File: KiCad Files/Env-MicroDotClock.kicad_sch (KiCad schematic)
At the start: 40 parts, among them IC1 IS31FL3730-QFLS2-TR, IC2 IS31FL3730-QFLS2-TR, IC3 IS31FL3730-QFLS2-TR, IC4 IS31FL3730-QFLS2-TR, M1 LTP-305G, M2 LTP-305G, M3 LTP-305G, M4 LTP-305G, M5 LTP-305G, M6 LTP-305G, M7 LTP-305G, M8 LTP-305G, Q1 2SC1815, SW1 SW_Push, SW2 SW_Push, SW3 SW_Push, SW4 SW_Push, U1 Pico, U2 DS1307Z+, Y1 32.768kHz 45kΩ 12.5

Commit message: small changes and fixes, among other adjustments.
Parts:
- removed Q1: 2SC1815, Package_TO_SOT_THT:TO-92_Inline, symbol Transistor_BJT:2SC1815
- removed U2: DS1307Z+, Package_SO:SOIC-8_3.9x4.9mm_P1.27mm, symbol Timer_RTC:DS1307Z+
- removed Y1: 32.768kHz 45kΩ 12.5, Crystal:Crystal_SMD_3225-4Pin_3.2x2.5mm_HandSoldering, symbol Device:Crystal_GND24
- added Q1: 2SC1815, Package_TO_SOT_SMD:SOT-23, symbol Transistor_BJT:BC817
- added U3: DS3231M, Package_SO:SOIC-16W_7.5x10.3mm_P1.27mm, symbol Timer_RTC:DS3231M
- C10: value 0805 15pF -> 0805 1uF
- C9: value 0805 15pF -> 0805 0.1uF
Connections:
- net +5V: now also C10.1, C9.1, U3.2 (VCC)
- net GND: now also C10.2, C9.2, Q1.2 (E), U3.10 (GND), U3.11 (GND), U3.12 (GND), U3.13 (GND), U3.5 (GND), U3.6 (GND), U3.7 (GND), U3.8 (GND), U3.9 (GND); no longer C10.1, C9.1
- net I2C_SCL: now also U3.16 (SCL)
- net I2C_SDA: now also U3.15 (SDA)
- net at R4.2: now also Q1.1 (B)
- net at BZ1.2 (+), R3.2: now also Q1.3 (C)
- net at BT1.1 (+): now also U3.14 (VBAT)

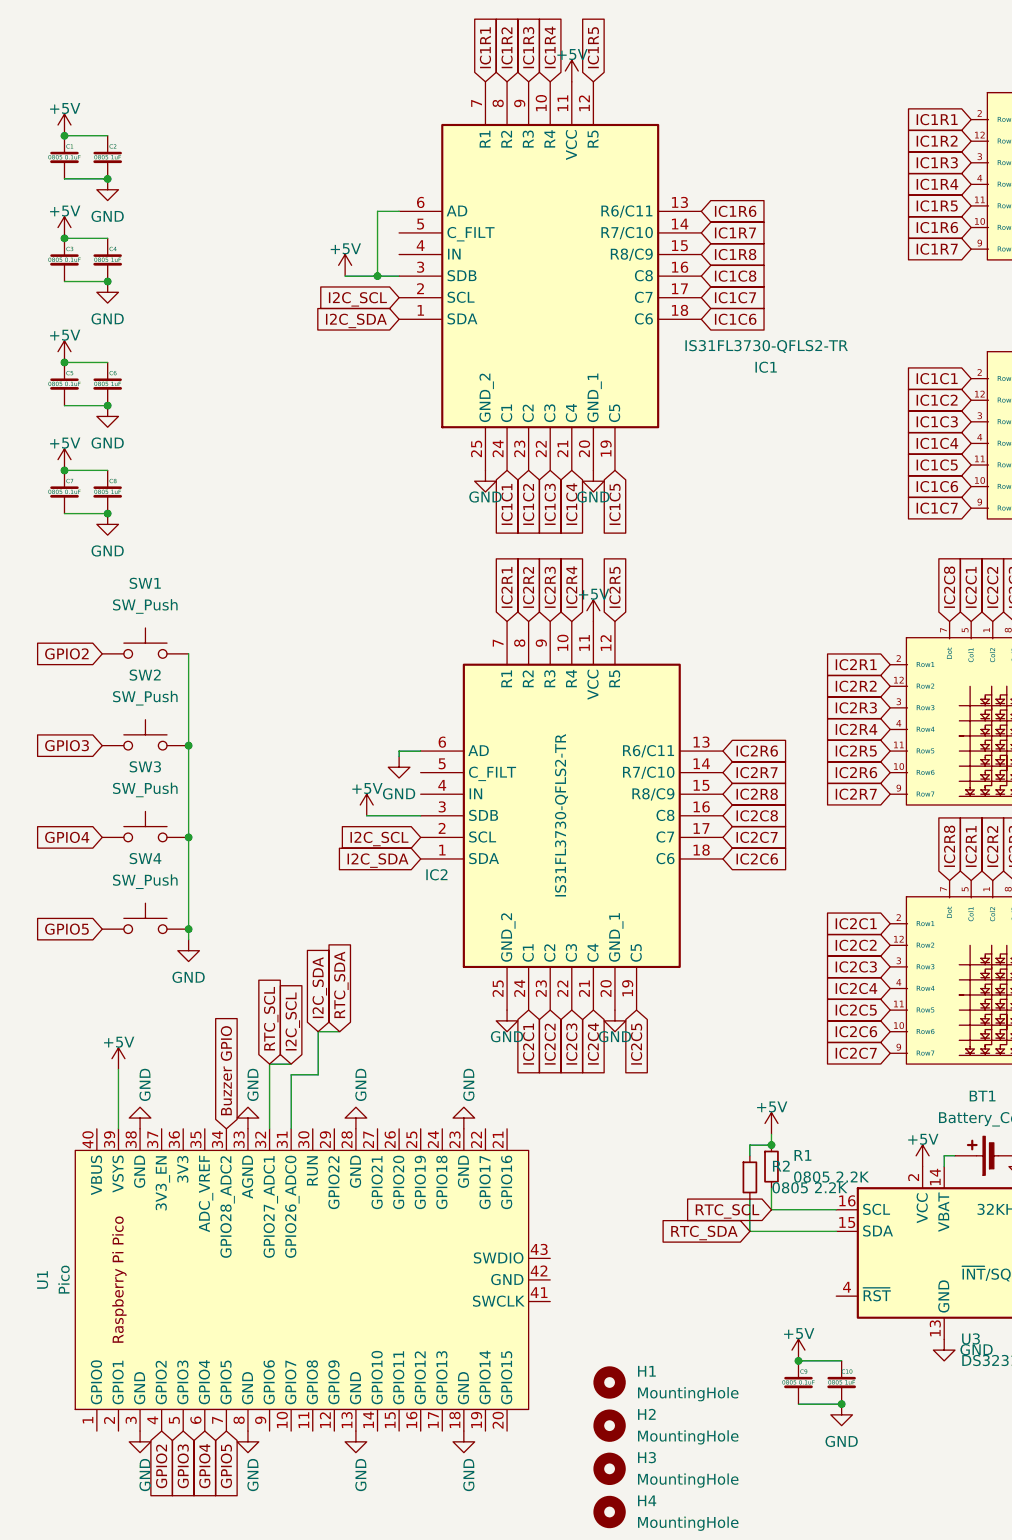
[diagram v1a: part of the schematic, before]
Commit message: Moved LTP305s up and the matrix ICs below the LTP305s
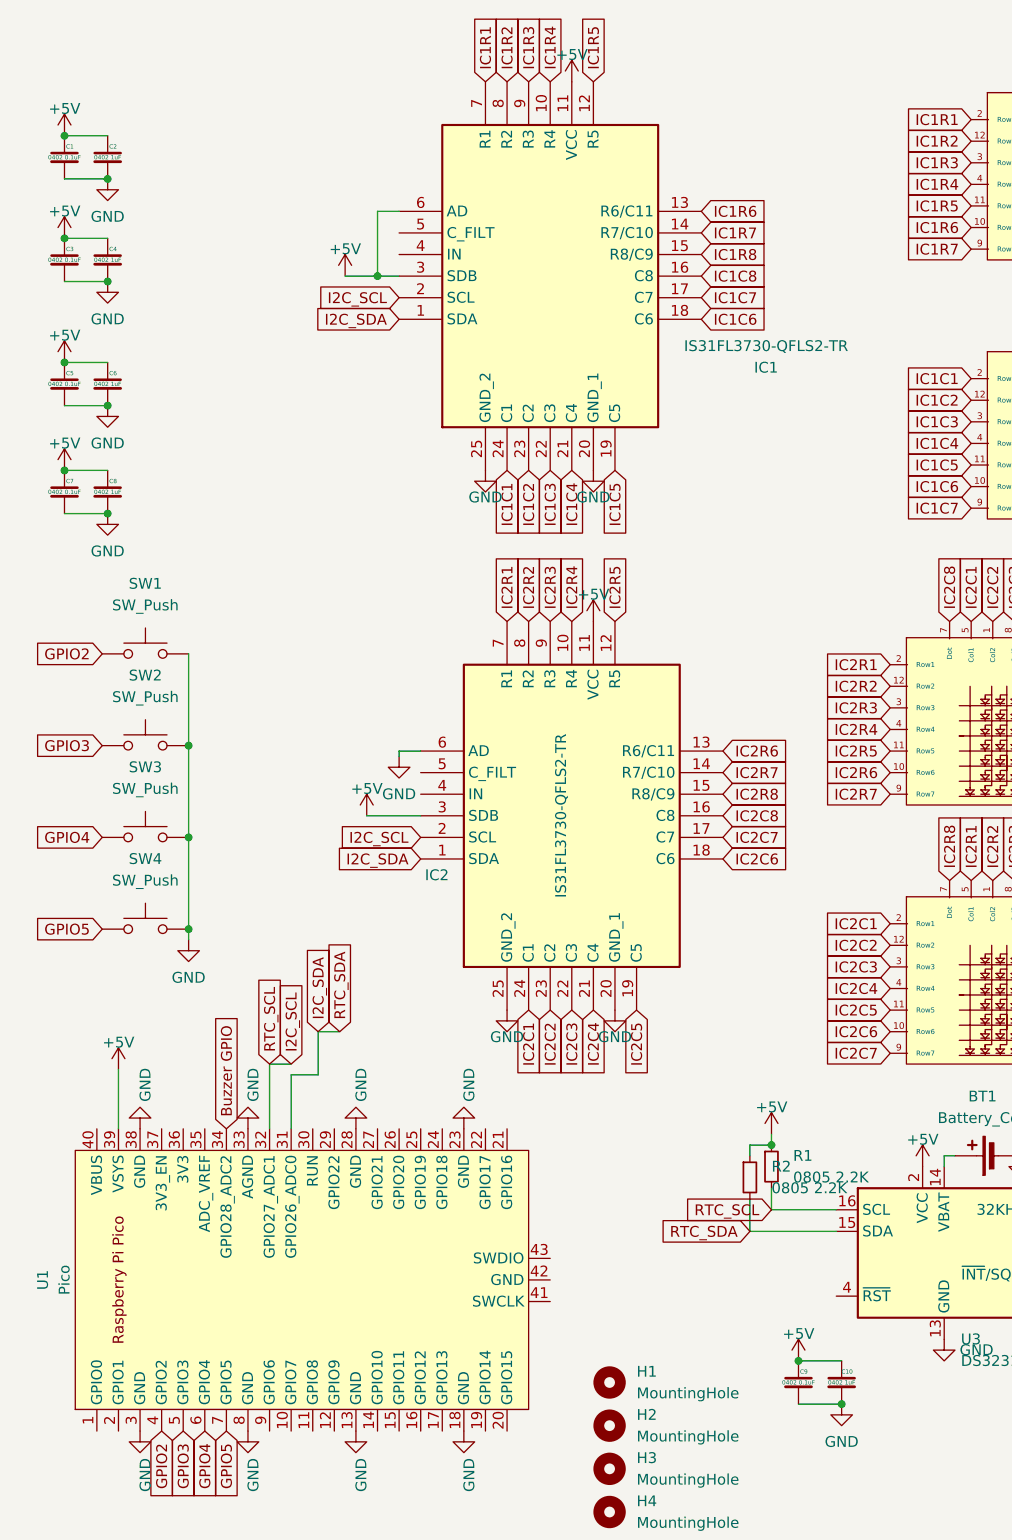
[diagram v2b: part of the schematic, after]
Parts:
- C1, C3, C5, C7, C9: value 0805 0.1uF -> 0402 0.1uF; footprint Capacitor_SMD:C_0805_2012Metric -> Capacitor_SMD:C_0402_1005Metric
- C10, C2, C4, C6, C8: value 0805 1uF -> 0402 1uF; footprint Capacitor_SMD:C_0805_2012Metric -> Capacitor_SMD:C_0402_1005Metric
- M1, M2, M3, M4, M5, M6, M7, M8: footprint LTP-305G:LTP-305G -> Package_DIP:DIP-14_W7.62mm_Socket
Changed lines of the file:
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@@
       (effects (font (size 0.5 0.5)))
     )
-    (property "Value" "0805 0.1uF" (at 104.775 180.34 0)
+    (property "Value" "0402 0.1uF" (at 104.775 180.34 0)
       (effects (font (size 0.5 0.5)))
     )
-    (property "Footprint" "Capacitor_SMD:C_0805_2012Metric" (at 104.775 180.34 0)
+    (property "Footprint" "Capacitor_SMD:C_0402_1005Metric" (at 104.775 180.34 0)
       (effects (font (size 1.27 1.27)) hide)
     )
@@
       (effects (font (size 0.5 0.5)))
     )
-    (property "Value" "0805 0.1uF" (at 18.415 75.565 0)
+    (property "Value" "0402 0.1uF" (at 18.415 75.565 0)
       (effects (font (size 0.5 0.5)))
     )
-    (property "Footprint" "Capacitor_SMD:C_0805_2012Metric" (at 18.415 75.565 0)
+    (property "Footprint" "Capacitor_SMD:C_0402_1005Metric" (at 18.415 75.565 0)
       (effects (font (size 1.27 1.27)) hide)
     )
@@
       (effects (font (size 0.5 0.5)))
     )
-    (property "Value" "0805 1uF" (at 109.855 180.34 0)
+    (property "Value" "0402 1uF" (at 109.855 180.34 0)
       (effects (font (size 0.5 0.5)))
     )
-    (property "Footprint" "Capacitor_SMD:C_0805_2012Metric" (at 109.855 180.34 0)
+    (property "Footprint" "Capacitor_SMD:C_0402_1005Metric" (at 109.855 180.34 0)
       (effects (font (size 1.27 1.27)) hide)
     )
@@
       (effects (font (size 0.5 0.5)))
     )
-    (property "Value" "0805 0.1uF" (at 18.415 36.195 0)
+    (property "Value" "0402 0.1uF" (at 18.415 36.195 0)
       (effects (font (size 0.5 0.5)))
     )
-    (property "Footprint" "Capacitor_SMD:C_0805_2012Metric" (at 18.415 36.195 0)
+    (property "Footprint" "Capacitor_SMD:C_0402_1005Metric" (at 18.415 36.195 0)
       (effects (font (size 1.27 1.27)) hide)
     )
@@
       (effects (font (size 0.5 0.5)))
     )
-    (property "Value" "0805 1uF" (at 23.495 62.865 0)
+    (property "Value" "0402 1uF" (at 23.495 62.865 0)
       (effects (font (size 0.5 0.5)))
     )
-    (property "Footprint" "Capacitor_SMD:C_0805_2012Metric" (at 23.495 62.865 0)
+    (property "Footprint" "Capacitor_SMD:C_0402_1005Metric" (at 23.495 62.865 0)
       (effects (font (size 1.27 1.27)) hide)
     )
@@
       (effects (font (size 1.27 1.27)) (justify left))
     )
-    (property "Footprint" "LTP-305G:LTP-305G" (at 263.525 140.335 0)
+    (property "Footprint" "Package_DIP:DIP-14_W7.62mm_Socket" (at 263.525 140.335 0)
       (effects (font (size 1.27 1.27)) hide)
     )
@@
       (effects (font (size 1.27 1.27)) (justify left))
     )
-    (property "Footprint" "LTP-305G:LTP-305G" (at 266.7 57.785 0)
+    (property "Footprint" "Package_DIP:DIP-14_W7.62mm_Socket" (at 266.7 57.785 0)
       (effects (font (size 1.27 1.27)) hide)
     )
@@
       (effects (font (size 1.27 1.27)) (justify left))
     )
-    (property "Footprint" "LTP-305G:LTP-305G" (at 263.525 109.855 0)
+    (property "Footprint" "Package_DIP:DIP-14_W7.62mm_Socket" (at 263.525 109.855 0)
       (effects (font (size 1.27 1.27)) hide)
     )
@@
       (effects (font (size 1.27 1.27)) (justify left))
     )
-    (property "Footprint" "LTP-305G:LTP-305G" (at 149.225 33.02 0)
+    (property "Footprint" "Package_DIP:DIP-14_W7.62mm_Socket" (at 149.225 33.02 0)
       (effects (font (size 1.27 1.27)) hide)
     )
@@
       (effects (font (size 1.27 1.27)) (justify left))
     )
-    (property "Footprint" "LTP-305G:LTP-305G" (at 139.7 97.155 0)
+    (property "Footprint" "Package_DIP:DIP-14_W7.62mm_Socket" (at 139.7 97.155 0)
       (effects (font (size 1.27 1.27)) hide)
     )
@@
       (effects (font (size 0.5 0.5)))
     )
-    (property "Value" "0805 1uF" (at 23.495 75.565 0)
+    (property "Value" "0402 1uF" (at 23.495 75.565 0)
       (effects (font (size 0.5 0.5)))
     )
-    (property "Footprint" "Capacitor_SMD:C_0805_2012Metric" (at 23.495 75.565 0)
+    (property "Footprint" "Capacitor_SMD:C_0402_1005Metric" (at 23.495 75.565 0)
       (effects (font (size 1.27 1.27)) hide)
     )
@@
       (effects (font (size 1.27 1.27)) (justify left))
     )
-    (property "Footprint" "LTP-305G:LTP-305G" (at 139.7 127.635 0)
+    (property "Footprint" "Package_DIP:DIP-14_W7.62mm_Socket" (at 139.7 127.635 0)
       (effects (font (size 1.27 1.27)) hide)
     )
@@
       (effects (font (size 1.27 1.27)) (justify left))
     )
-    (property "Footprint" "LTP-305G:LTP-305G" (at 266.7 27.305 0)
+    (property "Footprint" "Package_DIP:DIP-14_W7.62mm_Socket" (at 266.7 27.305 0)
       (effects (font (size 1.27 1.27)) hide)
     )
@@
       (effects (font (size 0.5 0.5)))
     )
-    (property "Value" "0805 1uF" (at 23.495 48.26 0)
+    (property "Value" "0402 1uF" (at 23.495 48.26 0)
       (effects (font (size 0.5 0.5)))
     )
-    (property "Footprint" "Capacitor_SMD:C_0805_2012Metric" (at 23.495 48.26 0)
+    (property "Footprint" "Capacitor_SMD:C_0402_1005Metric" (at 23.495 48.26 0)
       (effects (font (size 1.27 1.27)) hide)
     )
@@
       (effects (font (size 0.5 0.5)))
     )
-    (property "Value" "0805 1uF" (at 23.495 36.195 0)
+    (property "Value" "0402 1uF" (at 23.495 36.195 0)
       (effects (font (size 0.5 0.5)))
     )
-    (property "Footprint" "Capacitor_SMD:C_0805_2012Metric" (at 23.495 36.195 0)
+    (property "Footprint" "Capacitor_SMD:C_0402_1005Metric" (at 23.495 36.195 0)
       (effects (font (size 1.27 1.27)) hide)
     )
@@
       (effects (font (size 1.27 1.27)) (justify left))
     )
-    (property "Footprint" "LTP-305G:LTP-305G" (at 149.225 63.5 0)
+    (property "Footprint" "Package_DIP:DIP-14_W7.62mm_Socket" (at 149.225 63.5 0)
       (effects (font (size 1.27 1.27)) hide)
     )
@@
       (effects (font (size 0.5 0.5)))
     )
-    (property "Value" "0805 0.1uF" (at 18.415 62.865 0)
+    (property "Value" "0402 0.1uF" (at 18.415 62.865 0)
       (effects (font (size 0.5 0.5)))
     )
-    (property "Footprint" "Capacitor_SMD:C_0805_2012Metric" (at 18.415 62.865 0)
+    (property "Footprint" "Capacitor_SMD:C_0402_1005Metric" (at 18.415 62.865 0)
       (effects (font (size 1.27 1.27)) hide)
     )
@@
       (effects (font (size 0.5 0.5)))
     )
-    (property "Value" "0805 0.1uF" (at 18.415 48.26 0)
+    (property "Value" "0402 0.1uF" (at 18.415 48.26 0)
       (effects (font (size 0.5 0.5)))
     )
-    (property "Footprint" "Capacitor_SMD:C_0805_2012Metric" (at 18.415 48.26 0)
-      (effects (font (size 1.27 1.27)) hide)
-    )
+    (property "Footprint" "Capacitor_SMD:C_0402_1005Metric" (at 18.415 48.26 0)
+      (effects (font (size 1.27 1.27)) hide)
+    )

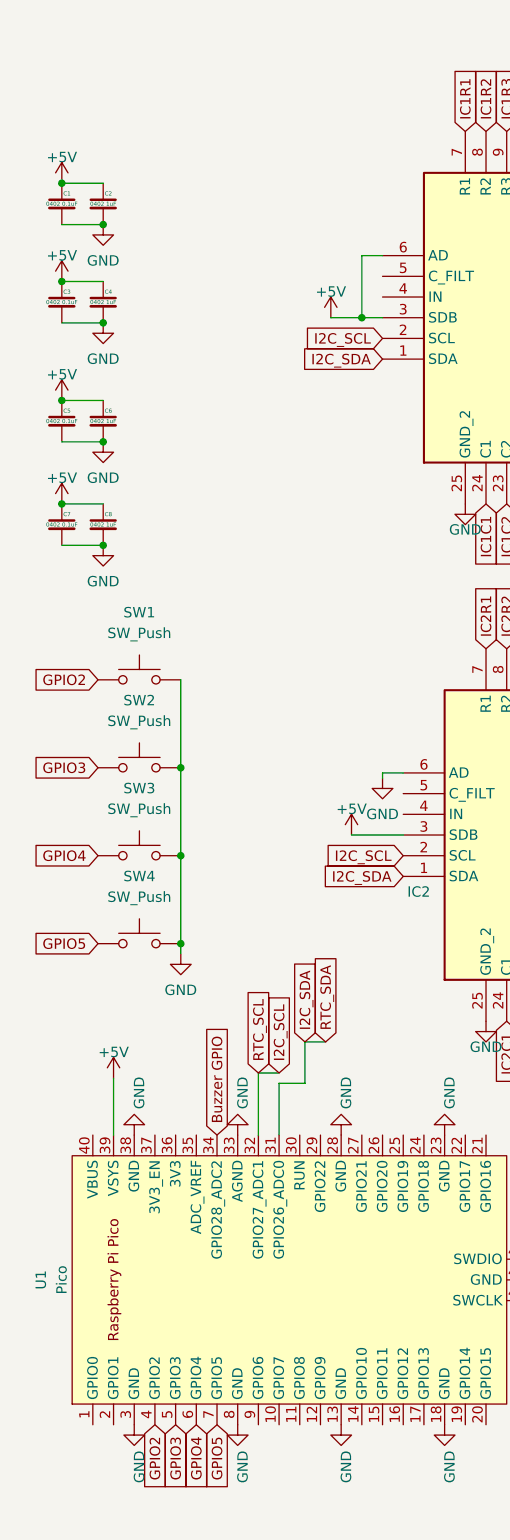
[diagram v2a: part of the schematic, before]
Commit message: added dip switch for summer time adjustment
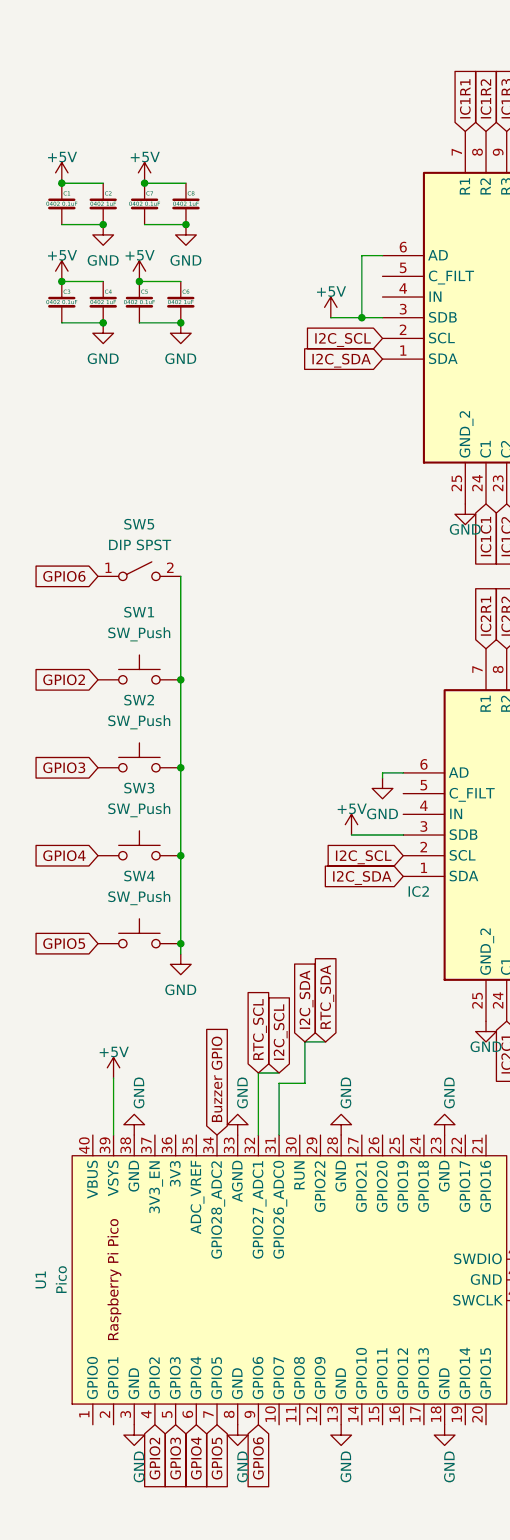
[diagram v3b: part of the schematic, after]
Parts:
- added SW5: DIP SPST, Button_Switch_SMD:SW_DIP_SPSTx01_Slide_9.78x4.72mm_W8.61mm_P2.54mm, symbol Switch:SW_SPST
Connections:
- net GND: now also SW5.2 (B)
- net GPIO6: now reaches U1.9 (GPIO6)
- net GPIO6: now also SW5.1 (A)
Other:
- moved on the sheet: C5, C6, C7, C8

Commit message: swapped dipswitch for smaller
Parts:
- SW5: footprint Button_Switch_SMD:SW_DIP_SPSTx01_Slide_9.78x4.72mm_W8.61mm_P2.54mm -> Button_Switch_SMD:SW_DIP_SPSTx01_Slide_Copal_CHS-01A_W5.08mm_P1.27mm_JPin
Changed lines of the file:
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@@
       (effects (font (size 1.27 1.27)))
     )
-    (property "Footprint" "Button_Switch_SMD:SW_DIP_SPSTx01_Slide_9.78x4.72mm_W8.61mm_P2.54mm" (at 27.94 81.915 0)
+    (property "Footprint" "Button_Switch_SMD:SW_DIP_SPSTx01_Slide_Copal_CHS-01A_W5.08mm_P1.27mm_JPin" (at 27.94 81.915 0)
       (effects (font (size 1.27 1.27)) hide)
     )

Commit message: made values more descriptive for SMTA
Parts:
- BT1: value Battery_Cell -> HLD-012
- BZ1: value Buzzer -> Buzzer 12.2Mm
- M1, M2, M3, M4, M5, M6, M7, M8: value LTP-305G -> Dip-14 Socket
- SW1, SW2, SW3, SW4: value SW_Push -> SKRK
- SW5: value DIP SPST -> DIP SPST W5.08mm_P1.27mm
- U1: value Pico -> Raspberry Pi Pico
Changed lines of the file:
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@@
       (effects (font (size 1.27 1.27)))
     )
-    (property "Value" "SW_Push" (at 27.94 121.285 0)
+    (property "Value" "SKRK" (at 27.94 121.285 0)
       (effects (font (size 1.27 1.27)))
     )
@@
       (effects (font (size 1.27 1.27)) (justify left))
     )
-    (property "Value" "Buzzer" (at 170.18 172.72 0)
+    (property "Value" "Buzzer 12.2Mm" (at 170.18 172.72 0)
       (effects (font (size 1.27 1.27)) (justify left))
     )
@@
       (effects (font (size 1.27 1.27)))
     )
-    (property "Value" "SW_Push" (at 27.94 110.49 0)
+    (property "Value" "SKRK" (at 27.94 110.49 0)
       (effects (font (size 1.27 1.27)))
     )
@@
       (effects (font (size 1.27 1.27)))
     )
-    (property "Value" "Battery_Cell" (at 126.4285 149.225 90)
+    (property "Value" "HLD-012" (at 126.4285 149.225 90)
       (effects (font (size 1.27 1.27)))
     )
@@
       (effects (font (size 1.27 1.27)) (justify left))
     )
-    (property "Value" "LTP-305G" (at 260.985 146.685 0)
+    (property "Value" "Dip-14 Socket" (at 260.985 146.685 0)
       (effects (font (size 1.27 1.27)) (justify left))
     )
@@
       (effects (font (size 1.27 1.27)) (justify left))
     )
-    (property "Value" "LTP-305G" (at 264.16 64.135 0)
+    (property "Value" "Dip-14 Socket" (at 264.16 64.135 0)
       (effects (font (size 1.27 1.27)) (justify left))
     )
@@
       (effects (font (size 1.27 1.27)) (justify left))
     )
-    (property "Value" "LTP-305G" (at 260.985 116.205 0)
+    (property "Value" "Dip-14 Socket" (at 260.985 116.205 0)
       (effects (font (size 1.27 1.27)) (justify left))
     )
@@
       (effects (font (size 1.27 1.27)))
     )
-    (property "Value" "Pico" (at 18.415 168.275 0)
+    (property "Value" "Raspberry Pi Pico" (at 18.415 168.275 0)
       (effects (font (size 1.27 1.27)))
     )
@@
       (effects (font (size 1.27 1.27)) (justify left))
     )
-    (property "Value" "LTP-305G" (at 146.685 39.37 0)
+    (property "Value" "Dip-14 Socket" (at 146.685 39.37 0)
       (effects (font (size 1.27 1.27)) (justify left))
     )
@@
       (effects (font (size 1.27 1.27)))
     )
-    (property "Value" "SW_Push" (at 27.94 88.9 0)
+    (property "Value" "SKRK" (at 27.94 88.9 0)
       (effects (font (size 1.27 1.27)))
     )
@@
       (effects (font (size 1.27 1.27)) (justify left))
     )
-    (property "Value" "LTP-305G" (at 137.16 103.505 0)
+    (property "Value" "Dip-14 Socket" (at 137.16 103.505 0)
       (effects (font (size 1.27 1.27)) (justify left))
     )
@@
       (effects (font (size 1.27 1.27)))
     )
-    (property "Value" "DIP SPST" (at 27.94 78.105 0)
+    (property "Value" "DIP SPST W5.08mm_P1.27mm" (at 27.94 78.105 0)
       (effects (font (size 1.27 1.27)))
     )
@@
       (effects (font (size 1.27 1.27)) (justify left))
     )
-    (property "Value" "LTP-305G" (at 137.16 133.985 0)
+    (property "Value" "Dip-14 Socket" (at 137.16 133.985 0)
       (effects (font (size 1.27 1.27)) (justify left))
     )
@@
       (effects (font (size 1.27 1.27)) (justify left))
     )
-    (property "Value" "LTP-305G" (at 264.16 33.655 0)
+    (property "Value" "Dip-14 Socket" (at 264.16 33.655 0)
       (effects (font (size 1.27 1.27)) (justify left))
     )
@@
       (effects (font (size 1.27 1.27)))
     )
-    (property "Value" "SW_Push" (at 27.94 99.695 0)
+    (property "Value" "SKRK" (at 27.94 99.695 0)
       (effects (font (size 1.27 1.27)))
     )
@@
       (effects (font (size 1.27 1.27)) (justify left))
     )
-    (property "Value" "LTP-305G" (at 146.685 69.85 0)
-      (effects (font (size 1.27 1.27)) (justify left))
-    )
+    (property "Value" "Dip-14 Socket" (at 146.685 69.85 0)
+      (effects (font (size 1.27 1.27)) (justify left))
+    )
